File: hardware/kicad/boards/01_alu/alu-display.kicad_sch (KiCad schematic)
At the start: 0 parts

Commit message: kicad: checkpoint; designed the alu display logic; clock circuit
Added registers for each display to ensure robustness and less worry about debugging screen, keeping focus on the alu board and other components
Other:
- added sheet display-counter (display-counter.kicad_sch)

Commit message: alu: completed all core schematics; DRC and ERC pending 🎉
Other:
- removed sheet text-clk
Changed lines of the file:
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@@
 	(wire
 		(pts
-			(xy 46.99 176.53) (xy 48.514 176.53)
+			(xy 48.26 176.53) (xy 45.72 176.53)
 		)
 		(stroke
@@
 	)
 	(label "text-clk"
-		(at 48.514 176.53 0)
+		(at 48.26 176.53 0)
 		(effects
 			(font
@@
 		)
 	)
+	(global_label "clk"
+		(shape output)
+		(at 45.72 176.53 180)
+		(fields_autoplaced yes)
+		(effects
+			(font
+				(size 1.27 1.27)
+			)
+			(justify right)
+		)
+		(property "Intersheetrefs" "${INTERSHEET_REFS}"
+			(at 39.9529 176.53 0)
+			(hide yes)
+			(show_name no)
+			(do_not_autoplace no)
+			(effects
+				(font
+					(size 1.27 1.27)
+				)
+				(justify right)
+			)
+		)
+	)
 	(sheet
 		(at 227.33 61.468)
@@
 			(project ""
 				(path "/70179ff6-7c16-4036-adf3-4ea9b5e0a238"
-					(page "")
+					(page "#")
 				)
 			)
@@
 			(project ""
 				(path "/70179ff6-7c16-4036-adf3-4ea9b5e0a238"
-					(page "")
+					(page "#")
 				)
 			)
@@
 			(project ""
 				(path "/70179ff6-7c16-4036-adf3-4ea9b5e0a238"
-					(page "")
+					(page "#")
 				)
 			)
@@
 			(project ""
 				(path "/70179ff6-7c16-4036-adf3-4ea9b5e0a238"
-					(page "")
+					(page "#")
 				)
 			)
@@
 			(project ""
 				(path "/70179ff6-7c16-4036-adf3-4ea9b5e0a238"
-					(page "")
+					(page "#")
 				)
 			)
@@
 			(project ""
 				(path "/70179ff6-7c16-4036-adf3-4ea9b5e0a238"
-					(page "")
+					(page "#")
 				)
 			)
@@
 			(project ""
 				(path "/70179ff6-7c16-4036-adf3-4ea9b5e0a238"
-					(page "")
+					(page "#")
 				)
 			)
@@
 			(project ""
 				(path "/70179ff6-7c16-4036-adf3-4ea9b5e0a238"
-					(page "")
+					(page "#")
 				)
 			)
@@
 			(project ""
 				(path "/70179ff6-7c16-4036-adf3-4ea9b5e0a238"
-					(page "")
+					(page "#")
 				)
 			)
@@
 			(project ""
 				(path "/70179ff6-7c16-4036-adf3-4ea9b5e0a238"
-					(page "")
+					(page "#")
 				)
 			)
@@
 			(project ""
 				(path "/70179ff6-7c16-4036-adf3-4ea9b5e0a238"
-					(page "")
+					(page "#")
 				)
 			)
@@
 			(project ""
 				(path "/70179ff6-7c16-4036-adf3-4ea9b5e0a238"
-					(page "")
+					(page "#")
 				)
 			)
@@
 			(project ""
 				(path "/70179ff6-7c16-4036-adf3-4ea9b5e0a238"
-					(page "")
+					(page "#")
 				)
 			)
@@
 			(project ""
 				(path "/70179ff6-7c16-4036-adf3-4ea9b5e0a238"
-					(page "")
+					(page "#")
 				)
 			)
@@
 			(project ""
 				(path "/70179ff6-7c16-4036-adf3-4ea9b5e0a238"
-					(page "")
+					(page "#")
 				)
 			)
@@
 	)
 	(sheet
-		(at 34.29 172.72)
-		(size 12.7 7.62)
-		(exclude_from_sim no)
-		(in_bom yes)
-		(on_board yes)
-		(dnp no)
-		(fields_autoplaced yes)
-		(stroke
-			(width 0.1524)
-			(type solid)
-		)
-		(fill
-			(color 0 0 0 0)
-		)
-		(property "Sheetname" "text-clk"
-			(at 34.29 172.0084 0)
-			(show_name no)
-			(do_not_autoplace no)
-			(effects
-				(font
-					(size 1.27 1.27)
-				)
-				(justify left bottom)
-			)
-		)
-		(property "Sheetfile" "text-clk.kicad_sch"
-			(at 34.29 180.9246 0)
-			(hide yes)
-			(show_name no)
-			(do_not_autoplace no)
-			(effects
-				(font
-					(size 1.27 1.27)
-				)
-				(justify left top)
-			)
-		)
-		(pin "clk" output
-			(at 46.99 176.53 0)
-			(effects
-				(font
-					(size 1.27 1.27)
-				)
-				(justify right)
-			)
-		)
-		(instances
-			(project ""
-				(path "/70179ff6-7c16-4036-adf3-4ea9b5e0a238"
-					(page "")
-				)
-			)
-			(project "alu-32b"
-				(path "/ddad1417-0afc-402d-a021-92fc87ddd78a/70179ff6-7c16-4036-adf3-4ea9b5e0a238"
-					(page "60")
-				)
-			)
-		)
-	)
-	(sheet
 		(at 163.83 98.044)
 		(size 16.002 28.448)
@@
 			(project ""
 				(path "/70179ff6-7c16-4036-adf3-4ea9b5e0a238"
-					(page "")
+					(page "#")
 				)
 			)
@@
 			(project ""
 				(path "/70179ff6-7c16-4036-adf3-4ea9b5e0a238"
-					(page "")
+					(page "#")
 				)
 			)
@@
 			(project ""
 				(path "/70179ff6-7c16-4036-adf3-4ea9b5e0a238"
-					(page "")
+					(page "#")
 				)
 			)
@@
 			(project ""
 				(path "/70179ff6-7c16-4036-adf3-4ea9b5e0a238"
-					(page "")
+					(page "#")
 				)
 			)
@@
 			(project ""
 				(path "/70179ff6-7c16-4036-adf3-4ea9b5e0a238"
-					(page "")
+					(page "#")
 				)
 			)
@@
 			(project ""
 				(path "/70179ff6-7c16-4036-adf3-4ea9b5e0a238"
-					(page "")
+					(page "#")
 				)
 			)
@@
 			(project ""
 				(path "/70179ff6-7c16-4036-adf3-4ea9b5e0a238"
-					(page "")
+					(page "#")
 				)
 			)
@@
 			(project ""
 				(path "/70179ff6-7c16-4036-adf3-4ea9b5e0a238"
-					(page "")
+					(page "#")
 				)
 			)
@@
 			(project ""
 				(path "/70179ff6-7c16-4036-adf3-4ea9b5e0a238"
-					(page "")
+					(page "#")
 				)
 			)
@@
 			(project ""
 				(path "/70179ff6-7c16-4036-adf3-4ea9b5e0a238"
-					(page "")
+					(page "#")
 				)
 			)
@@
 			(project ""
 				(path "/70179ff6-7c16-4036-adf3-4ea9b5e0a238"
-					(page "")
+					(page "#")
 				)
 			)
@@
 			(project ""
 				(path "/70179ff6-7c16-4036-adf3-4ea9b5e0a238"
-					(page "")
+					(page "#")
 				)
 			)
@@
 			(project ""
 				(path "/70179ff6-7c16-4036-adf3-4ea9b5e0a238"
-					(page "")
+					(page "#")
 				)
 			)
@@
 			(project ""
 				(path "/70179ff6-7c16-4036-adf3-4ea9b5e0a238"
-					(page "")
+					(page "#")
 				)
 			)
@@
 			(project ""
 				(path "/70179ff6-7c16-4036-adf3-4ea9b5e0a238"
-					(page "")
+					(page "#")
 				)
 			)
@@
 			(project ""
 				(path "/70179ff6-7c16-4036-adf3-4ea9b5e0a238"
-					(page "")
+					(page "#")
 				)
 			)
@@
 			(project ""
 				(path "/70179ff6-7c16-4036-adf3-4ea9b5e0a238"
-					(page "")
+					(page "#")
 				)
 			)

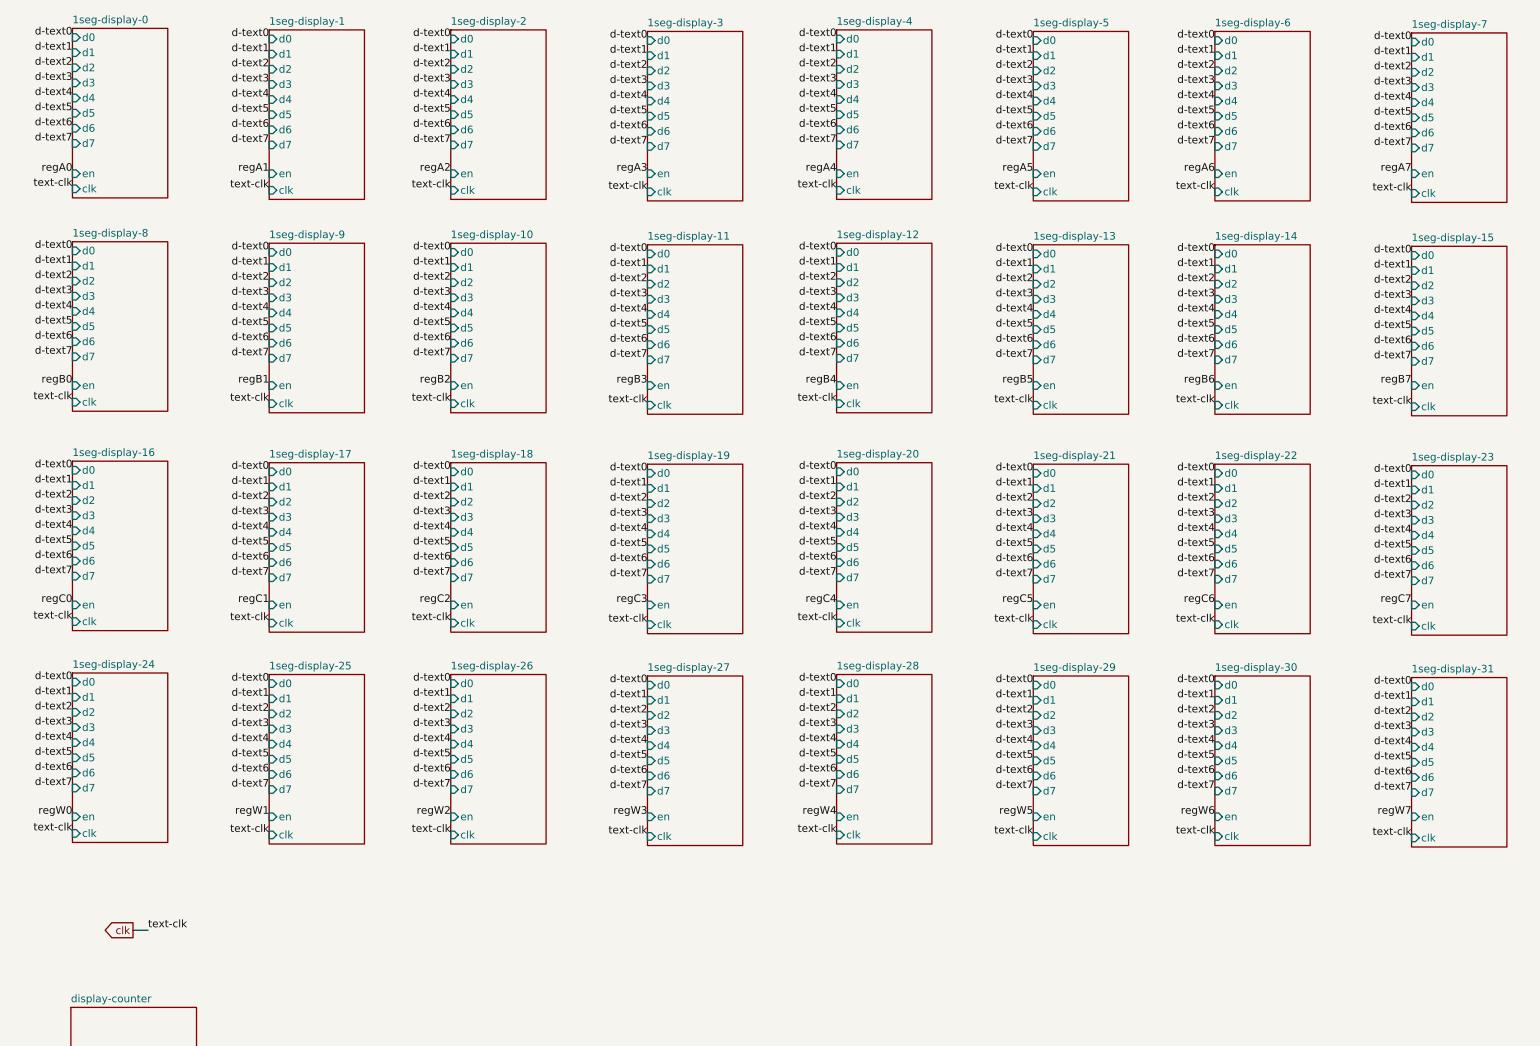
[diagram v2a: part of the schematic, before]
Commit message: refactor: improved global labeling and reduced ERC from 300+ to 6 power flags and minor connector in errors
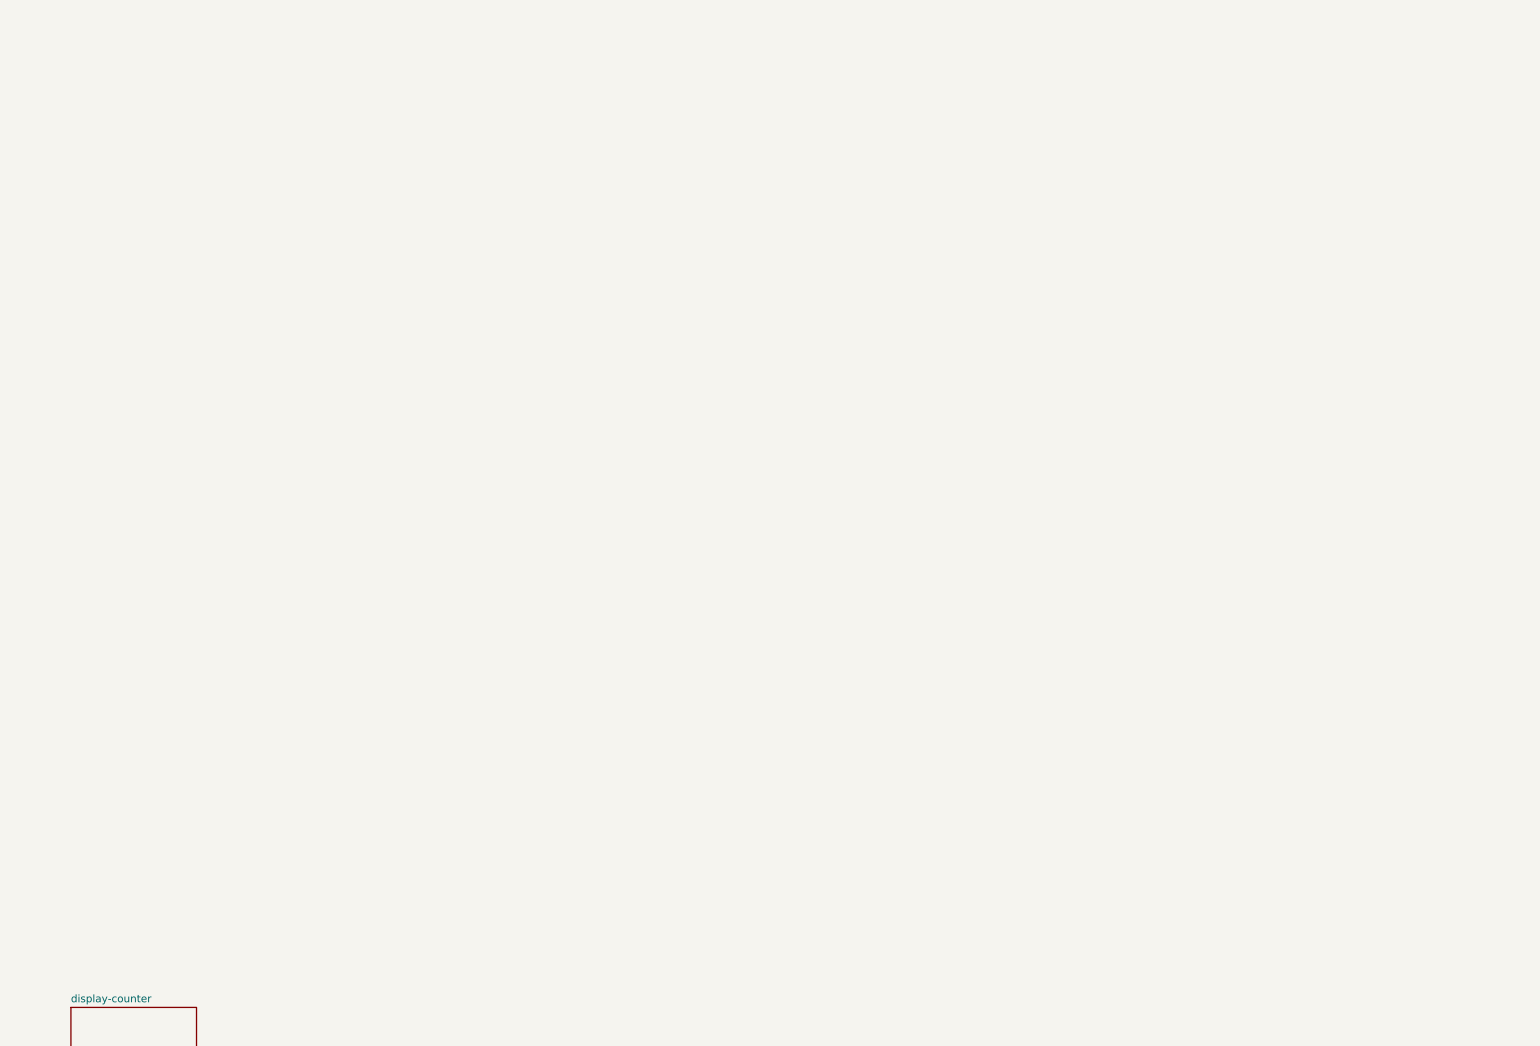
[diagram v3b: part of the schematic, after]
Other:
- removed sheet 1seg-display-0
- removed sheet 1seg-display-1
- removed sheet 1seg-display-10
- removed sheet 1seg-display-11
- removed sheet 1seg-display-12
- removed sheet 1seg-display-13
- removed sheet 1seg-display-14
- removed sheet 1seg-display-15
- removed sheet 1seg-display-16
- removed sheet 1seg-display-17
- removed sheet 1seg-display-18
- removed sheet 1seg-display-19
- removed sheet 1seg-display-2
- removed sheet 1seg-display-20
- removed sheet 1seg-display-21
- removed sheet 1seg-display-22
- removed sheet 1seg-display-23
- removed sheet 1seg-display-24
- removed sheet 1seg-display-25
- removed sheet 1seg-display-26
- removed sheet 1seg-display-27
- removed sheet 1seg-display-28
- removed sheet 1seg-display-29
- removed sheet 1seg-display-3
- removed sheet 1seg-display-30
- removed sheet 1seg-display-31
- removed sheet 1seg-display-4
- removed sheet 1seg-display-5
- removed sheet 1seg-display-6
- removed sheet 1seg-display-7
- removed sheet 1seg-display-8
- removed sheet 1seg-display-9

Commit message: fix: fixed erc to 0; remaining are warnings about labeling which are being fixed; latest alu schematics pending decoration and organization
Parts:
- added C169, C170, C171, C172, C173, C174, C175, C176: 100nF, Capacitor_SMD:C_0805_2012Metric, symbol Device:C
- added U169, U173: 74LS154, Package_SO:SOIC-24W_7.5x15.4mm_P1.27mm, symbol 74xx:74LS154
- added U170, U172: 74LS163, Package_SO:SOIC-16_3.9x9.9mm_P1.27mm, symbol 74xx:74LS163
- added U171: 74AHC1G04, Package_TO_SOT_SMD:SOT-23-5, symbol 74xGxx:74AHC1G04
- added U174: KM28C64A, Package_DIP:DIP-28_W15.24mm, symbol Memory_EEPROM:KM28C64A
- added U175, U176: 74LS153, Package_SO:SOIC-16_3.9x9.9mm_P1.27mm, symbol 74xx:74LS153
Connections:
- new net A0: U175.6 (I0a)
- new net A1: U175.10 (I0b)
- new net A2: U176.6 (I0a)
- new net A3: U176.10 (I0b)
- new net B0: U175.5 (I1a)
- new net B1: U175.11 (I1b)
- new net B2: U176.5 (I1a)
- new net B3: U176.11 (I1b)
- new net C0: U175.4 (I2a)
- new net C1: U175.12 (I2b)
- new net C2: U176.4 (I2a)
- new net C3: U176.12 (I2b)
- new net GND: C169.2, C170.2, C171.2, C172.2, C173.2, C174.2, C175.2, C176.2, U169.12 (GND), U169.18 (E0), U170.3 (D0), U170.4 (D1), U170.5 (D2), U170.6 (D3), U170.8 (GND), U171.3 (GND), U172.3 (D0), U172.4 (D1), U172.5 (D2), U172.6 (D3), U172.8 (GND), U173.12 (GND), U173.18 (E0), U174.14 (GND), U174.2 (A12), U174.20 (~{CE}), U174.21 (A10), U174.22 (~{OE}), U174.23 (A11), U174.24 (A9), U174.25 (A8), U174.3 (A7), U174.4 (A6), U174.5 (A5), U174.6 (A4), U175.1 (Ea), U175.15 (Eb), U175.8 (GND), U176.1 (Ea), U176.15 (Eb), U176.8 (GND)
- new net VCC: C169.1, C170.1, C171.1, C172.1, C173.1, C174.1, C175.1, C176.1, U169.24 (VCC), U170.1 (~{MR}), U170.10 (CET), U170.16 (VCC), U170.7 (CEP), U170.9 (~{PE}), U171.5 (VCC), U172.1 (~{MR}), U172.16 (VCC), U172.9 (~{PE}), U173.24 (VCC), U174.27 (~{WE}), U174.28 (VCC), U175.16 (VCC), U176.16 (VCC)
- new net W0: U175.3 (I3a)
- new net W1: U175.13 (I3b)
- new net W2: U176.3 (I3a)
- new net W3: U176.13 (I3b)
- new net d-text0: U174.11 (I/O0)
- new net d-text1: U174.12 (I/O1)
- new net d-text2: U174.13 (I/O2)
- new net d-text3: U174.15 (I/O3)
- new net d-text4: U174.16 (I/O4)
- new net d-text5: U174.17 (I/O5)
- new net d-text6: U174.18 (I/O6)
- new net d-text7: U174.19 (I/O7)
- new net q0: U169.23 (A0), U170.14 (Q0), U173.23 (A0)
- new net q1: U169.22 (A1), U170.13 (Q1), U173.22 (A1)
- new net q2: U169.21 (A2), U170.12 (Q2), U173.21 (A2)
- new net q3: U169.20 (A3), U170.11 (Q3), U173.20 (A3), U175.14 (S0), U176.14 (S0)
- new net q4: U169.19 (E1), U171.2, U172.14 (Q0), U175.2 (S1), U176.2 (S1)
- new net regA0: U169.1 (S0)
- new net regA1: U169.2 (S1)
- new net regA2: U169.3 (S2)
- new net regA3: U169.4 (S3)
- new net regA4: U169.5 (S4)
- new net regA5: U169.6 (S5)
- new net regA6: U169.7 (S6)
- new net regA7: U169.8 (S7)
- new net regB0: U169.9 (S8)
- new net regB1: U169.10 (S9)
- new net regB2: U169.11 (S10)
- new net regB3: U169.13 (S11)
- new net regB4: U169.14 (S12)
- new net regB5: U169.15 (S13)
- new net regB6: U169.16 (S14)
- new net regB7: U169.17 (S15)
- new net regC0: U173.1 (S0)
- new net regC1: U173.2 (S1)
- new net regC2: U173.3 (S2)
- new net regC3: U173.4 (S3)
- new net regC4: U173.5 (S4)
- new net regC5: U173.6 (S5)
- new net regC6: U173.7 (S6)
- new net regC7: U173.8 (S7)
- new net regW0: U173.9 (S8)
- new net regW1: U173.10 (S9)
- new net regW2: U173.11 (S10)
- new net regW3: U173.13 (S11)
- new net regW4: U173.14 (S12)
- new net regW5: U173.15 (S13)
- new net regW6: U173.16 (S14)
- new net regW7: U173.17 (S15)
- new net sig0: U174.10 (A0), U175.7 (Za)
- new net sig1: U174.9 (A1), U175.9 (Zb)
- new net sig2: U174.8 (A2), U176.7 (Za)
- new net sig3: U174.7 (A3), U176.9 (Zb)
- new net tc0: U170.15 (TC), U172.10 (CET), U172.7 (CEP)
- new net textclk: U170.2 (CP), U172.2 (CP)
- new net ~q4: U171.4, U173.19 (E1)
- no-connect marks 0 -> 4
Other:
- removed sheet display-counter
- added sheet display-clock (text-clk.kicad_sch)
- added sheet mux4_8to1-0 (../../modules/mux/mux-74xx/mux4_8to1.kicad_sch)
- added sheet mux4_8to1-1 (../../modules/mux/mux-74xx/mux4_8to1.kicad_sch)
- added sheet mux4_8to1-2 (../../modules/mux/mux-74xx/mux4_8to1.kicad_sch)
- added sheet mux4_8to1-3 (../../modules/mux/mux-74xx/mux4_8to1.kicad_sch)
- added sheet seg-disp0 (1-seg-display.kicad_sch)
- added sheet seg-disp1 (1-seg-display.kicad_sch)
- added sheet seg-disp10 (1-seg-display.kicad_sch)
- added sheet seg-disp11 (1-seg-display.kicad_sch)
- added sheet seg-disp12 (1-seg-display.kicad_sch)
- added sheet seg-disp13 (1-seg-display.kicad_sch)
- added sheet seg-disp14 (1-seg-display.kicad_sch)
- added sheet seg-disp15 (1-seg-display.kicad_sch)
- added sheet seg-disp16 (1-seg-display.kicad_sch)
- added sheet seg-disp17 (1-seg-display.kicad_sch)
- added sheet seg-disp18 (1-seg-display.kicad_sch)
- added sheet seg-disp19 (1-seg-display.kicad_sch)
- added sheet seg-disp20 (1-seg-display.kicad_sch)
- added sheet seg-disp21 (1-seg-display.kicad_sch)
- added sheet seg-disp22 (1-seg-display.kicad_sch)
- added sheet seg-disp23 (1-seg-display.kicad_sch)
- added sheet seg-disp24 (1-seg-display.kicad_sch)
- added sheet seg-disp25 (1-seg-display.kicad_sch)
- added sheet seg-disp26 (1-seg-display.kicad_sch)
- added sheet seg-disp27 (1-seg-display.kicad_sch)
- added sheet seg-disp28 (1-seg-display.kicad_sch)
- added sheet seg-disp29 (1-seg-display.kicad_sch)
- added sheet seg-disp3 (1-seg-display.kicad_sch)
- added sheet seg-disp30 (1-seg-display.kicad_sch)
- added sheet seg-disp31 (1-seg-display.kicad_sch)
- added sheet seg-disp32 (1-seg-display.kicad_sch)
- added sheet seg-disp4 (1-seg-display.kicad_sch)
- added sheet seg-disp5 (1-seg-display.kicad_sch)
- added sheet seg-disp6 (1-seg-display.kicad_sch)
- added sheet seg-disp7 (1-seg-display.kicad_sch)
- added sheet seg-disp8 (1-seg-display.kicad_sch)
- added sheet seg-disp9 (1-seg-display.kicad_sch)

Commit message: feat: designed ALU board with 0 ERC errors or warnings 🎉
Final review of logical correctness and footprints and then routing begins
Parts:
- renumbered C169 to C5901, C173 to C5902, C175 to C5903, C176 to C5904, C170 to C5905, C172 to C5906, C171 to C5907, C174 to C5908, U169 to U5901, U173 to U5902, U175 to U5903, U176 to U5904, U170 to U5905, U172 to U5906, U171 to U5907, U174 to U5908
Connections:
- net A0: no longer U5903.6 (I0a)
- net A1: no longer U5903.10 (I0b)
- net A2: no longer U5904.6 (I0a)
- net A3: no longer U5904.10 (I0b)
- net B0: no longer U5903.5 (I1a)
- net B1: no longer U5903.11 (I1b)
- net B2: no longer U5904.5 (I1a)
- net B3: no longer U5904.11 (I1b)
- net C0: no longer U5903.4 (I2a)
- net C1: no longer U5903.12 (I2b)
- net C2: no longer U5904.4 (I2a)
- net C3: no longer U5904.12 (I2b)
- net W0 renamed W-disp0
- net W1 renamed W-disp1
- net W2 renamed W-disp2
- net W3 renamed W-disp3
- new net A-disp0: U5903.6 (I0a)
- new net A-disp1: U5903.10 (I0b)
- new net A-disp2: U5904.6 (I0a)
- new net A-disp3: U5904.10 (I0b)
- new net B-disp0: U5903.5 (I1a)
- new net B-disp1: U5903.11 (I1b)
- new net B-disp2: U5904.5 (I1a)
- new net B-disp3: U5904.11 (I1b)
- new net C-disp0: U5903.4 (I2a)
- new net C-disp1: U5903.12 (I2b)
- new net C-disp2: U5904.4 (I2a)
- new net C-disp3: U5904.12 (I2b)
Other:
- removed sheet mux4_8to1-0
- removed sheet mux4_8to1-1
- removed sheet mux4_8to1-2
- removed sheet mux4_8to1-3
- added sheet mux4_8to1-4 (../../modules/mux/mux-74xx/mux4_8to1.kicad_sch)
- added sheet mux4_8to1-5 (../../modules/mux/mux-74xx/mux4_8to1.kicad_sch)
- added sheet mux4_8to1-6 (../../modules/mux/mux-74xx/mux4_8to1.kicad_sch)
- added sheet mux4_8to1-7 (../../modules/mux/mux-74xx/mux4_8to1.kicad_sch)
- moved on the sheet: U5903

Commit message: arch: added LEDs, override switches; fixed errors and warnings to 0
ready for routing after logical coherence check
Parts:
- renumbered C5901 to C168, C5905 to C169, C5907 to C170, C5906 to C171, C5902 to C172, C5908 to C173, C5903 to C174, C5904 to C175, U5901 to U168, U5905 to U169, U5907 to U170, U5906 to U171, U5902 to U172, U5908 to U173, U5903 to U174, U5904 to U175

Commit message: chore: cleanup and annotation  of alu subboards; hygiene before routing
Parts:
- renumbered C168 to C173, C169 to C174, C170 to C175, C171 to C176, C172 to C177, C173 to C178, C174 to C179, C175 to C180, U168 to U173, U169 to U174, U170 to U175, U171 to U176, U172 to U177, U173 to U178, U174 to U179, U175 to U180
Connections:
- net regA4: no longer names the net of U173.5 (S4)
- net regA5: no longer names the net of U173.6 (S5)
- net regA6: no longer names the net of U173.7 (S6)
- net regA7: no longer names the net of U173.8 (S7)
- net regB4: no longer names the net of U173.14 (S12)
- net regB5: no longer names the net of U173.15 (S13)
- net regB6: no longer names the net of U173.16 (S14)
- net regB7: no longer names the net of U173.17 (S15)
- net regC4: no longer names the net of U177.5 (S4)
- net regC5: no longer names the net of U177.6 (S5)
- net regC6: no longer names the net of U177.7 (S6)
- net regC7: no longer names the net of U177.8 (S7)
- no-connect marks 4 -> 68
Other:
- removed sheet seg-disp13
- removed sheet seg-disp14
- removed sheet seg-disp15
- removed sheet seg-disp16
- removed sheet seg-disp21
- removed sheet seg-disp22
- removed sheet seg-disp23
- removed sheet seg-disp24
- removed sheet seg-disp5
- removed sheet seg-disp6
- removed sheet seg-disp7
- removed sheet seg-disp8
- added sheet mux4_4to1 (../../modules/mux/mux-74xx/mux4_8to1.kicad_sch)
